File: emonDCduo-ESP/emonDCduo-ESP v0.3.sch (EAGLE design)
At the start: 89 parts, among them Q1 16Mhz XT49M-2016M, U1_TQFP ATMEGA328P

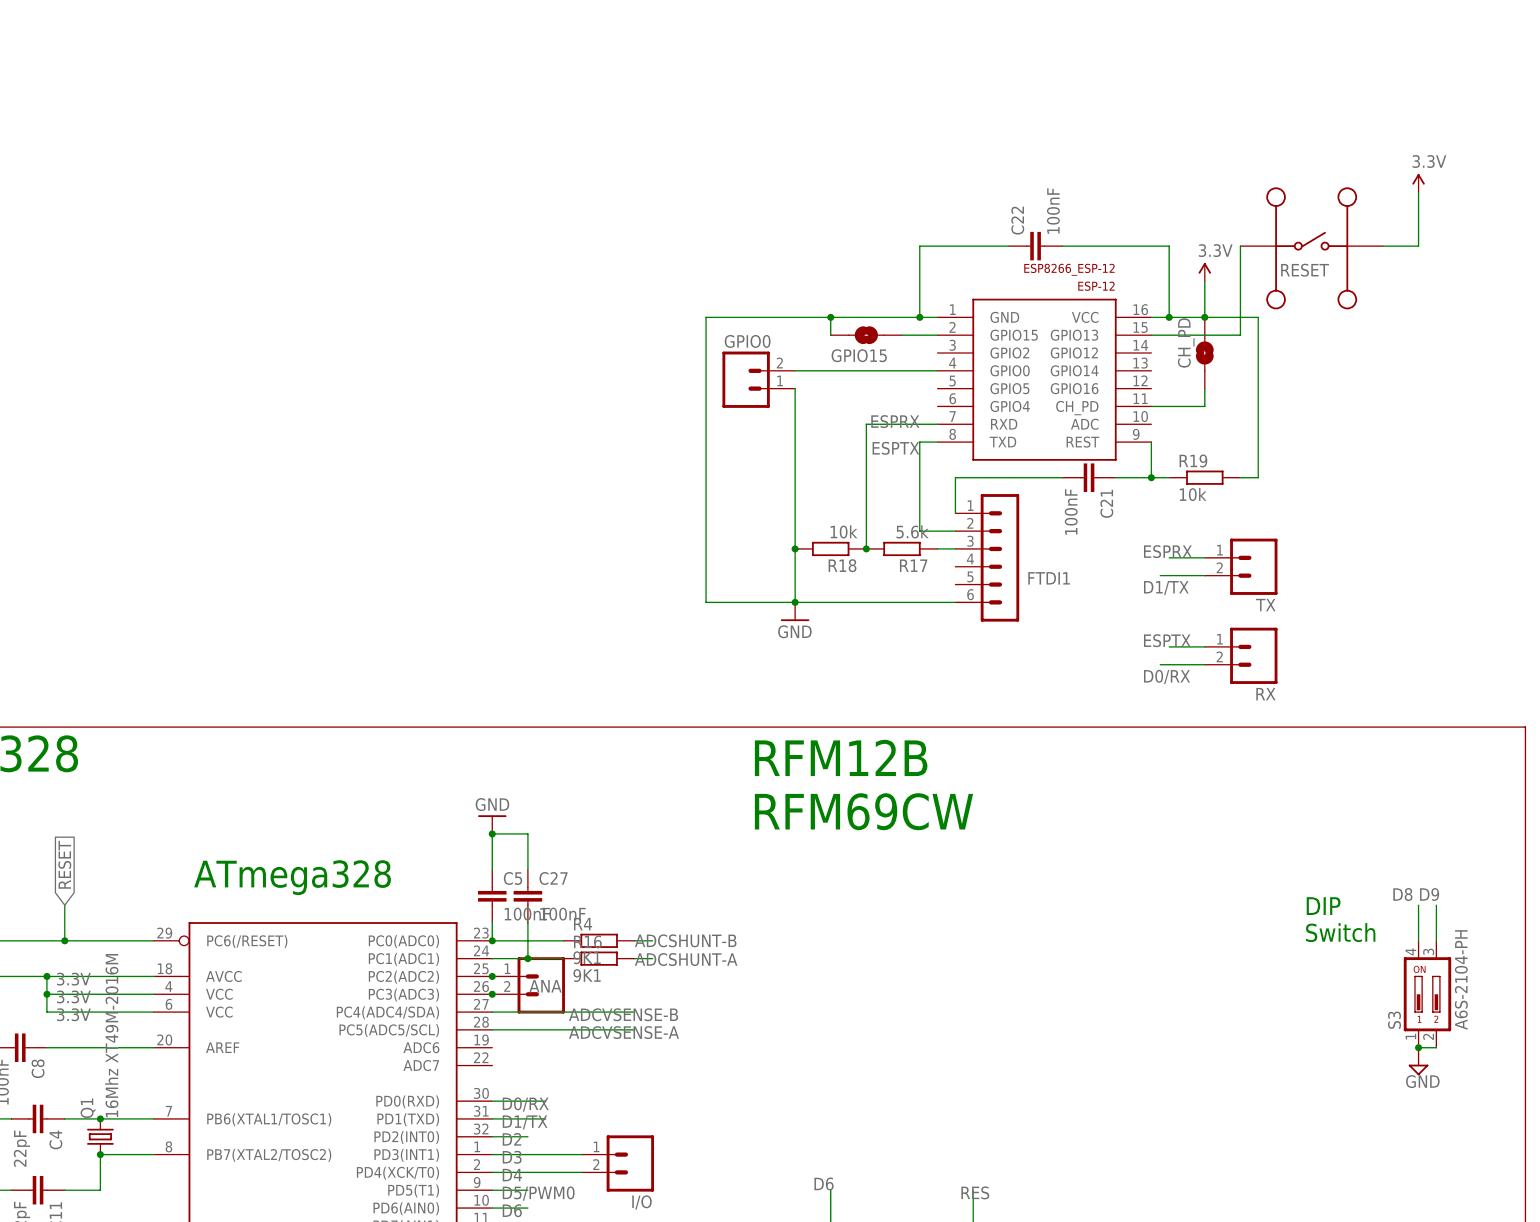
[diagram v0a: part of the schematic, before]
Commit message: SD CARD TO DUO
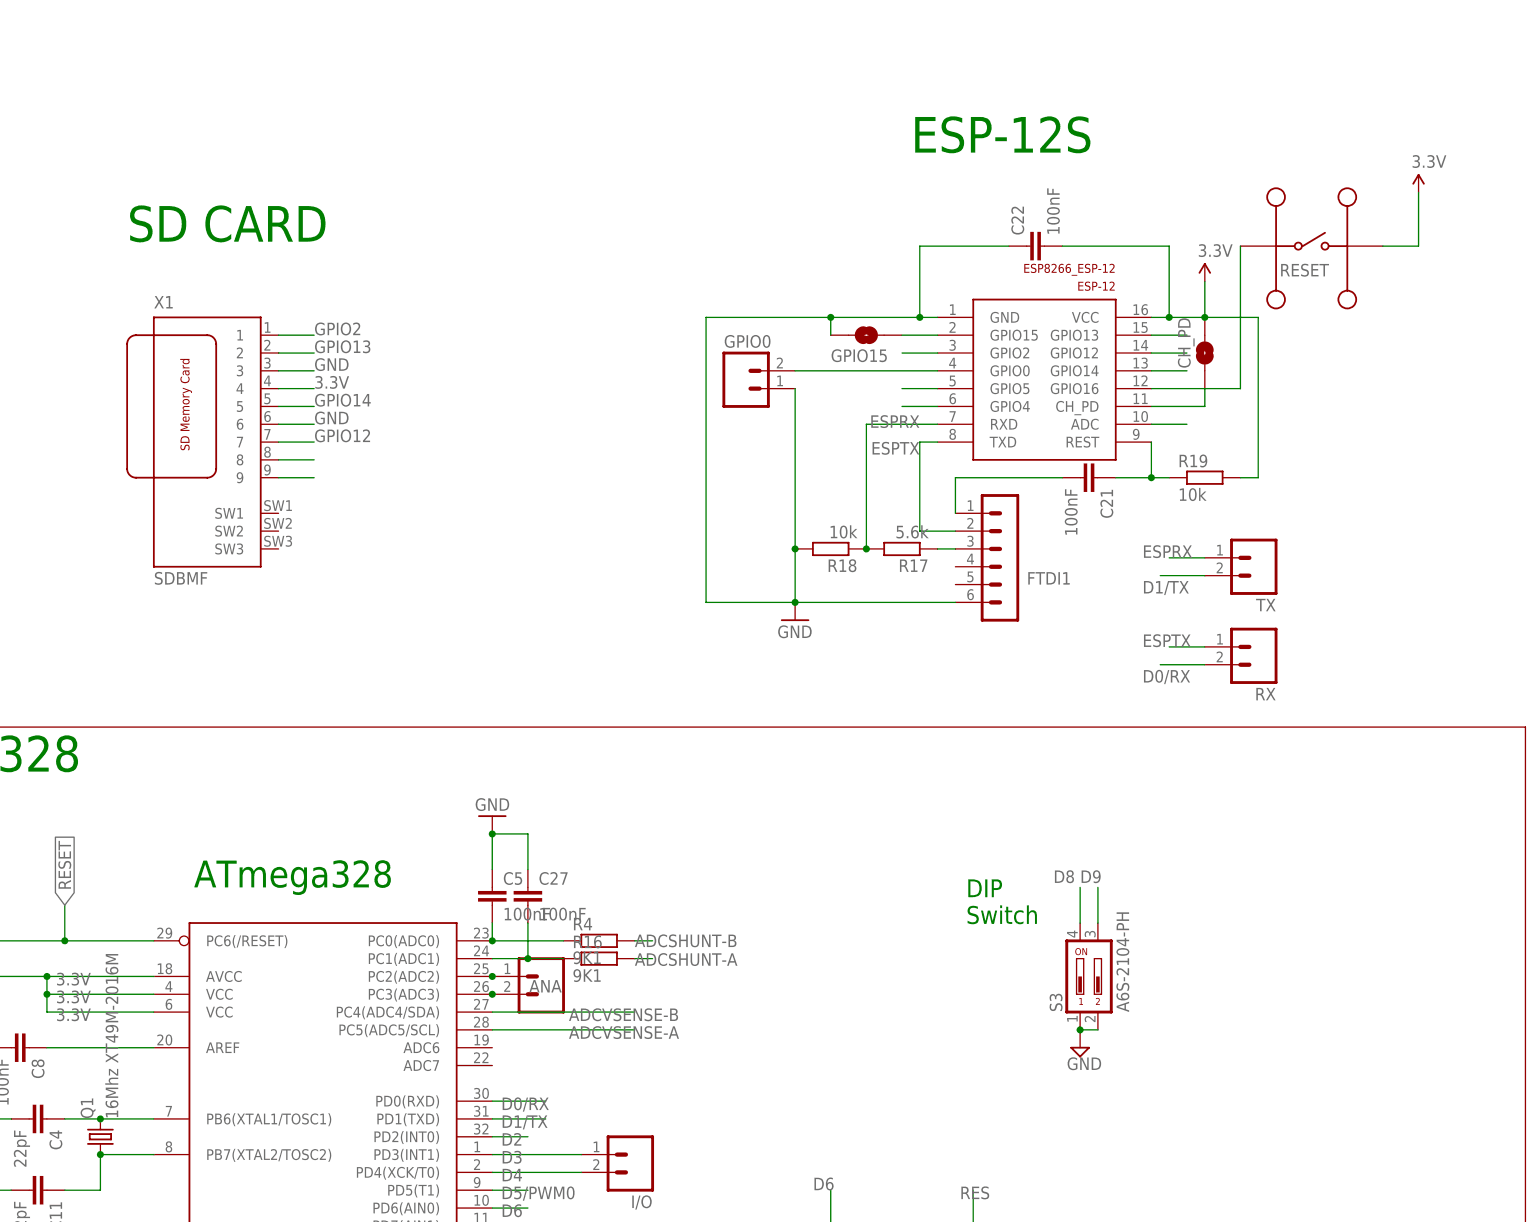
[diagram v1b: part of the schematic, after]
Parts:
- added X1: SDBMF, farnell:SDBMF
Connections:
- removed net RESET1: ESP-12.GPIO13, MC1.P$1
- new net GPIO12: ESP-12.GPIO12, X1.7
- new net GPIO13: ESP-12.GPIO13, X1.2
- new net GPIO14: ESP-12.GPIO14, X1.5
- new net GPIO16: ESP-12.GPIO16, MC1.P$1
- new net GPIO2: ESP-12.GPIO2, X1.1
- new net GPIO4: ESP-12.GPIO4
- new net GPIO5: ESP-12.GPIO5
- new net N$33: X1.8
- new net N$34: X1.9
- new net N$44: ESP-12.ADC
- net 3.3V: now also X1.4
- net GND: now also X1.3, X1.6
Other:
- note added: "ESP-12S"
- note added: "SD CARD"
- note removed: "RFM12B RFM69CW"
- moved on the sheet: S3
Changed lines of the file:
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@@
 <part name="J3" library="SparkFun-Connectors" deviceset="CONN_03" device=""/>
 <part name="J4" library="SparkFun-Connectors" deviceset="CONN_03" device=""/>
+<part name="X1" library="farnell" deviceset="SDBMF" device=""/>
 </parts>
 <sheets>
@@
 <text x="-83.82" y="194.31" size="1.778" layer="91">Hardware design files are licensed under the Creative Commons Attribution-ShareAlike 3.0 Unported License</text>
 <text x="94.615" y="370.84" size="3.81" layer="91">ATmega328</text>
-<text x="173.99" y="379.095" size="5.08" layer="91">RFM12B
-RFM69CW</text>
-<text x="252.984" y="363.093" size="2.54" layer="91">DIP
+<text x="204.724" y="365.633" size="2.54" layer="91">DIP
 Switch</text>
 <text x="189.23" y="285.115" size="5.08" layer="91">FTDI OPTO ISO</text>
@@
 <wire x1="116.84" y1="222.25" x2="36.322" y2="222.25" width="0.1524" layer="94"/>
 <wire x1="36.322" y1="222.25" x2="36.322" y2="265.43" width="0.1524" layer="94"/>
+<text x="196.85" y="475.615" size="5.08" layer="91">ESP-12S</text>
+<text x="85.09" y="462.915" size="5.08" layer="91">SD CARD</text>
 </plain>
 <instances>
@@
 <instance part="P+3" gate="G$1" x="256.54" y="317.5"/>
 <instance part="C2" gate="G$1" x="203.2" y="238.76"/>
-<instance part="S3" gate="G$1" x="269.24" y="355.6">
-<attribute name="OC_FARNELL" x="269.24" y="355.6" size="1.778" layer="96" display="off"/>
-<attribute name="MF" x="269.24" y="355.6" size="1.778" layer="96" display="off"/>
-<attribute name="MPN" x="269.24" y="355.6" size="1.778" layer="96" display="off"/>
-</instance>
-<instance part="SUPPLY3" gate="GND" x="269.24" y="345.44"/>
+<instance part="S3" gate="G$1" x="220.98" y="358.14">
+<attribute name="OC_FARNELL" x="220.98" y="358.14" size="1.778" layer="96" display="off"/>
+<attribute name="MF" x="220.98" y="358.14" size="1.778" layer="96" display="off"/>
+<attribute name="MPN" x="220.98" y="358.14" size="1.778" layer="96" display="off"/>
+</instance>
+<instance part="SUPPLY3" gate="GND" x="220.98" y="347.98"/>
 <instance part="AGND11" gate="VR1" x="71.12" y="302.26"/>
 <instance part="SHUNTMON-B" gate="G$1" x="-68.58" y="340.36" rot="R90">
@@
 <instance part="J3" gate="J$1" x="-96.52" y="335.28" rot="R270"/>
 <instance part="J4" gate="J$1" x="-96.52" y="337.82" rot="R90"/>
+<instance part="X1" gate="G$1" x="101.6" y="431.8"/>
 </instances>
 <busses>
@@
 <pinref part="SUPPLY3" gate="GND" pin="GND"/>
 <pinref part="S3" gate="G$1" pin="2"/>
-<wire x1="271.78" y1="347.98" x2="269.24" y2="347.98" width="0.1524" layer="91"/>
-<junction x="269.24" y="347.98"/>
+<wire x1="223.52" y1="350.52" x2="220.98" y2="350.52" width="0.1524" layer="91"/>
+<junction x="220.98" y="350.52"/>
 </segment>
 <segment>
@@
 <pinref part="C10" gate="A" pin="2"/>
 </segment>
+<segment>
+<pinref part="X1" gate="G$1" pin="3"/>
+<wire x1="106.68" y1="444.5" x2="111.76" y2="444.5" width="0.1524" layer="91"/>
+<label x="111.76" y="444.5" size="1.778" layer="95"/>
+</segment>
+<segment>
+<pinref part="X1" gate="G$1" pin="6"/>
+<wire x1="106.68" y1="436.88" x2="111.76" y2="436.88" width="0.1524" layer="91"/>
+<label x="111.76" y="436.88" size="1.778" layer="95"/>
+</segment>
 </net>
 <net name="ADCVSENSE-A" class="0">
@@
 <pinref part="P+2" gate="G$1" pin="3.3V"/>
 </segment>
+<segment>
+<pinref part="X1" gate="G$1" pin="4"/>
+<wire x1="106.68" y1="441.96" x2="111.76" y2="441.96" width="0.1524" layer="91"/>
+<label x="111.76" y="441.96" size="1.778" layer="95"/>
+</segment>
 </net>
 <net name="RESET" class="0">
@@
 <segment>
 <pinref part="S3" gate="G$1" pin="4"/>
-<wire x1="269.24" y1="363.22" x2="269.24" y2="368.3" width="0.1524" layer="91"/>
-<label x="265.43" y="368.935" size="1.778" layer="95"/>
+<wire x1="220.98" y1="365.76" x2="220.98" y2="370.84" width="0.1524" layer="91"/>
+<label x="217.17" y="371.475" size="1.778" layer="95"/>
 </segment>
 </net>
@@
 <segment>
 <pinref part="S3" gate="G$1" pin="3"/>
-<wire x1="271.78" y1="363.22" x2="271.78" y2="368.3" width="0.1524" layer="91"/>
-<label x="269.24" y="368.935" size="1.778" layer="95"/>
+<wire x1="223.52" y1="365.76" x2="223.52" y2="370.84" width="0.1524" layer="91"/>
+<label x="220.98" y="371.475" size="1.778" layer="95"/>
 </segment>
 <segment>
@@
 </segment>
 </net>
-<net name="RESET1" class="0">
-<segment>
-<pinref part="ESP-12" gate="G$1" pin="GPIO13"/>
-<wire x1="243.84" y1="462.28" x2="243.84" y2="449.58" width="0.1524" layer="91"/>
-<wire x1="243.84" y1="449.58" x2="231.14" y2="449.58" width="0.1524" layer="91"/>
-<pinref part="MC1" gate="G$1" pin="P$1"/>
-</segment>
-</net>
 <net name="ESPTX" class="0">
 <segment>
@@
 </segment>
 </net>
+<net name="GPIO2" class="0">
+<segment>
+<pinref part="X1" gate="G$1" pin="1"/>
+<wire x1="106.68" y1="449.58" x2="111.76" y2="449.58" width="0.1524" layer="91"/>
+<label x="111.76" y="449.58" size="1.778" layer="95"/>
+</segment>
+<segment>
+<pinref part="ESP-12" gate="G$1" pin="GPIO2"/>
+<wire x1="200.66" y1="447.04" x2="195.58" y2="447.04" width="0.1524" layer="91"/>
+</segment>
+</net>
+<net name="N$33" class="0">
+<segment>
+<pinref part="X1" gate="G$1" pin="8"/>
+<wire x1="106.68" y1="431.8" x2="111.76" y2="431.8" width="0.1524" layer="91"/>
+</segment>
+</net>
+<net name="N$34" class="0">
+<segment>
+<pinref part="X1" gate="G$1" pin="9"/>
+<wire x1="106.68" y1="429.26" x2="111.76" y2="429.26" width="0.1524" layer="91"/>
+</segment>
+</net>
+<net name="GPIO5" class="0">
+<segment>
+<pinref part="ESP-12" gate="G$1" pin="GPIO5"/>
+<wire x1="200.66" y1="441.96" x2="195.58" y2="441.96" width="0.1524" layer="91"/>
+</segment>
+</net>
+<net name="GPIO4" class="0">
+<segment>
+<pinref part="ESP-12" gate="G$1" pin="GPIO4"/>
+<wire x1="200.66" y1="439.42" x2="195.58" y2="439.42" width="0.1524" layer="91"/>
+</segment>
+</net>
+<net name="GPIO16" class="0">
+<segment>
+<pinref part="ESP-12" gate="G$1" pin="GPIO16"/>
+<pinref part="MC1" gate="G$1" pin="P$1"/>
+<wire x1="231.14" y1="441.96" x2="243.84" y2="441.96" width="0.1524" layer="91"/>
+<wire x1="243.84" y1="441.96" x2="243.84" y2="462.28" width="0.1524" layer="91"/>
+</segment>
+</net>
+<net name="GPIO14" class="0">
+<segment>
+<pinref part="ESP-12" gate="G$1" pin="GPIO14"/>
+<wire x1="231.14" y1="444.5" x2="236.22" y2="444.5" width="0.1524" layer="91"/>
+</segment>
+<segment>
+<pinref part="X1" gate="G$1" pin="5"/>
+<wire x1="106.68" y1="439.42" x2="111.76" y2="439.42" width="0.1524" layer="91"/>
+<label x="111.76" y="439.42" size="1.778" layer="95"/>
+</segment>
+</net>
+<net name="GPIO12" class="0">
+<segment>
+<pinref part="ESP-12" gate="G$1" pin="GPIO12"/>
+<wire x1="231.14" y1="447.04" x2="236.22" y2="447.04" width="0.1524" layer="91"/>
+</segment>
+<segment>
+<pinref part="X1" gate="G$1" pin="7"/>
+<wire x1="106.68" y1="434.34" x2="111.76" y2="434.34" width="0.1524" layer="91"/>
+<label x="111.76" y="434.34" size="1.778" layer="95"/>
+</segment>
+</net>
+<net name="N$44" class="0">
+<segment>
+<pinref part="ESP-12" gate="G$1" pin="ADC"/>
+<wire x1="231.14" y1="436.88" x2="236.22" y2="436.88" width="0.1524" layer="91"/>
+</segment>
+</net>
+<net name="GPIO13" class="0">
+<segment>
+<pinref part="ESP-12" gate="G$1" pin="GPIO13"/>
+<wire x1="231.14" y1="449.58" x2="236.22" y2="449.58" width="0.1524" layer="91"/>
+</segment>
+<segment>
+<pinref part="X1" gate="G$1" pin="2"/>
+<wire x1="106.68" y1="447.04" x2="111.76" y2="447.04" width="0.1524" layer="91"/>
+<label x="111.76" y="447.04" size="1.778" layer="95"/>
+</segment>
+</net>

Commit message: short write protect pins
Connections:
- new net N$11: X1.SW2, X1.SW3
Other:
- note added: "NON-ISOLATED UART BACKUP FOR TESTING"
- note added: "Short to write protect:unlock"
- note added: "emonDC v0.3 : based on emonTx v3.4 by Glyn Hudson and Trystan Lea OpenEnergyMonitor.org"
- note removed: "emonDC v0.3 OpenEnergyMonitor.org"
- moved on the sheet: C17, C2, FTDI/UART, ISOLATED-UART, OK1, OK2, OK3, R11, R12, R3, R6, R7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

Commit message: micro sd card library
pinout in schematic TBD
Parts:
- added U$1: 47219-2001_MICROSD, 47219-2001_SD_MICRO:47219-2001_MICROSD
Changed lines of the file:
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@@
 <part name="J4" library="SparkFun-Connectors" deviceset="CONN_03" device=""/>
 <part name="X1" library="farnell" deviceset="SDBMF" device=""/>
+<part name="U$1" library="47219-2001_SD_MICRO" deviceset="47219-2001_MICROSD" device=""/>
 </parts>
 <sheets>
@@
 <instance part="J4" gate="J$1" x="-96.52" y="337.82" rot="R90"/>
 <instance part="X1" gate="G$1" x="101.6" y="431.8"/>
+<instance part="U$1" gate="G$1" x="55.88" y="424.18"/>
 </instances>
 <busses>
